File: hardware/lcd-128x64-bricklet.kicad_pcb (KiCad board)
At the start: 2 copper layers, 95 x 55 mm, 44 parts, among them P1 CON-SENSOR2, P2 Debug, P3 BOOT, P4 CON_4Wire_ER-TP028-1, Q1 2N7002, U1 XMC130024, U2 TSC2046E, U3 LCD-ERC12864, U4 DRILL, U5 DRILL, U6 DRILL, U7 DRILL

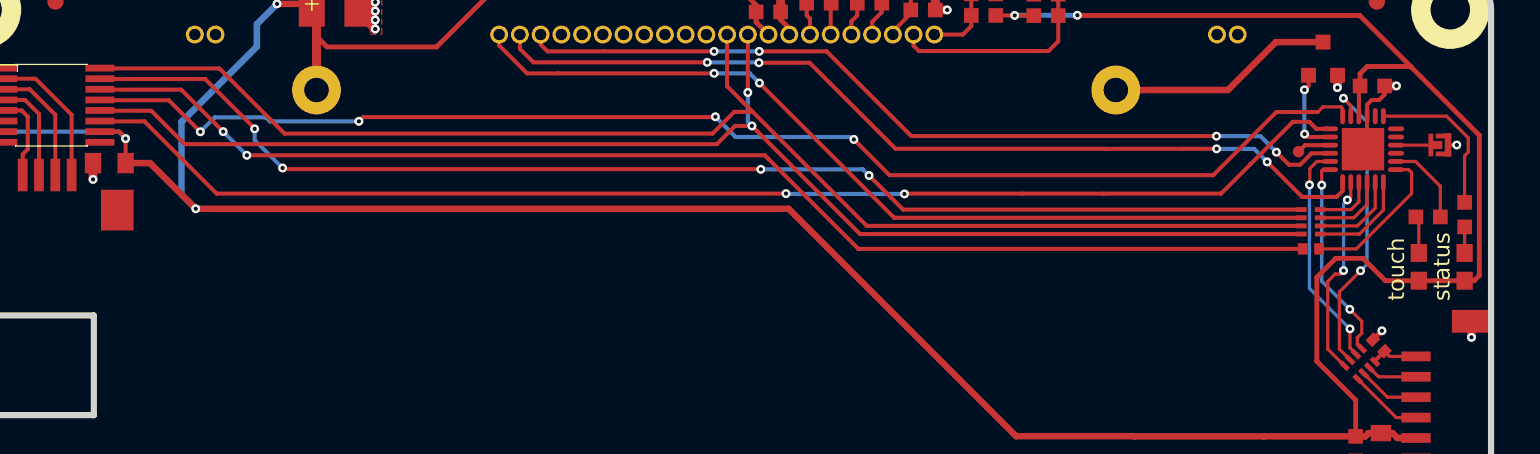
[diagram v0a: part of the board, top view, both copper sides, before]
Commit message: Change SPI pins because of flashing failure
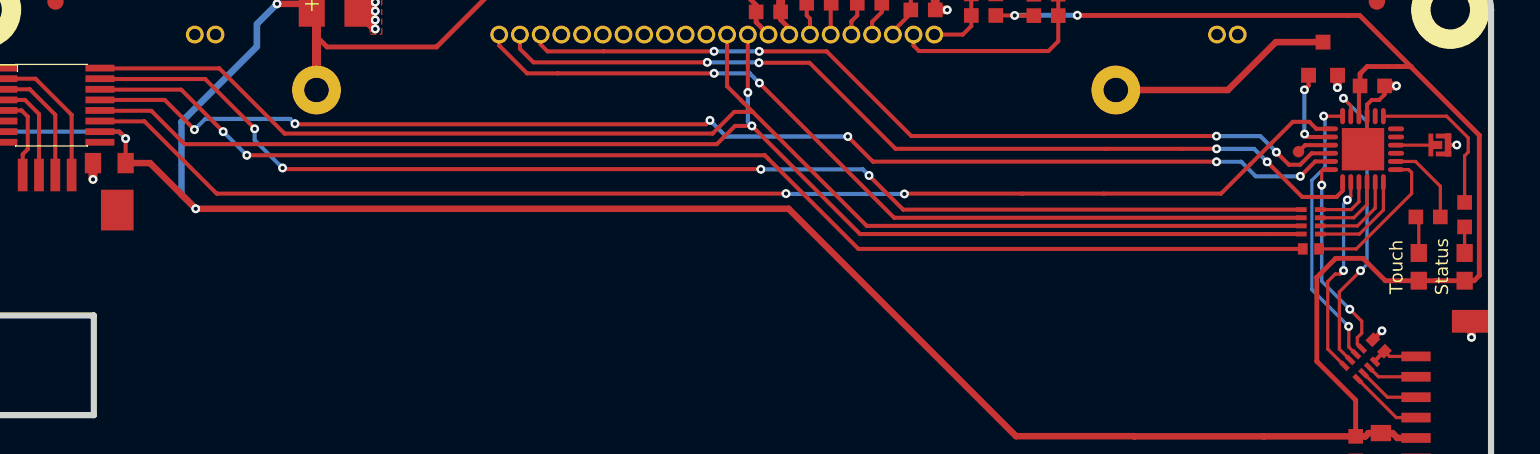
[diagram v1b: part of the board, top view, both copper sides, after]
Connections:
- U1 pad 12: TS-BUSY -> S-MOSI
- U1 pad 17: S-MOSI -> TS-BUSY
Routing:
- net S-MOSI: track 14.0 -> 17.7 mm
- net TS-BUSY: track 81.1 -> 78.5 mm, vias 4 -> 6
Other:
- board text added: "Status"
- board text added: "Touch"
- board text removed: "status"
- board text removed: "touch"
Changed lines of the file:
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@@
     (thickness 1.6)
     (drawings 16)
-    (tracks 477)
+    (tracks 479)
     (zones 0)
     (modules 44)
@@
   (title_block
     (title "LCD 128x64 Bricklet")
-    (date 2017-12-05)
+    (date 2018-01-25)
     (rev 1.0)
     (company "Tinkerforge GmbH")
     (comment 1 "Licensed under CERN OHL v.1.1")
-    (comment 2 "Copyright (©) 2017, L.Lauer <lukas@tinkerforge.com>")
+    (comment 2 "Copyright (©) 2018, L.Lauer <lukas@tinkerforge.com>")
   )
   (layers
@@
   )
   (setup
-    (last_trace_width 0.25)
+    (last_trace_width 0.2)
     (user_trace_width 0.2)
     (user_trace_width 0.25)
@@
     (visible_elements FFFFFF7F)
     (pcbplotparams
-      (layerselection 0x00030_80000001)
+      (layerselection 0x010fc_80000001)
       (usegerberextensions false)
       (excludeedgelayer true)
@@
       (psnegative false)
       (psa4output false)
-      (plotreference true)
-      (plotvalue true)
+      (plotreference false)
+      (plotvalue false)
       (plotinvisibletext false)
       (padsonsilk false)
@@
       (outputformat 1)
       (mirror false)
-      (drillshape 1)
+      (drillshape 0)
       (scaleselection 1)
       (outputdirectory ""))
@@
       (net 28 S-CLK))
     (pad 12 smd oval (at 1.25 2.025 270) (size 1 0.3) (layers F.Cu F.Paste F.Mask)
-      (net 38 TS-BUSY))
+      (net 27 S-MOSI))
     (pad 13 smd oval (at 2.025 1.25 180) (size 1 0.3) (layers F.Cu F.Paste F.Mask)
       (net 39 PENIRQ))
@@
       (net 40 LCD-CD))
     (pad 17 smd oval (at 2.025 -0.75 180) (size 1 0.3) (layers F.Cu F.Paste F.Mask)
-      (net 27 S-MOSI))
+      (net 38 TS-BUSY))
     (pad 18 smd oval (at 2.025 -1.25 180) (size 1 0.3) (layers F.Cu F.Paste F.Mask)
       (net 26 S-MISO))
@@
   (gr_line (start 101.25 88.65) (end 101.25 82.54) (angle 90) (layer Edge.Cuts) (width 0.381))
   (gr_line (start 95.25 82.54) (end 95.25 88.65) (angle 90) (layer Edge.Cuts) (width 0.381))
-  (gr_text touch (at 181.1 79.7 90) (layer F.SilkS)
-    (effects (font (size 1 1) (thickness 0.15)))
+  (gr_text Touch (at 181.1 79.57 90) (layer F.SilkS)
+    (effects (font (size 0.8 0.8) (thickness 0.15)))
   )
   (gr_text "LCD 128x64 1.0" (at 180.5 108.37) (layer F.SilkS)
@@
   (gr_arc (start 184.4 113.8) (end 186.9 113.8) (angle 90) (layer Edge.Cuts) (width 0.381))
   (gr_arc (start 184.4 63.8) (end 184.4 61.3) (angle 90) (layer Edge.Cuts) (width 0.381))
-  (gr_text status (at 183.89 79.55 90) (layer F.SilkS)
-    (effects (font (size 1 1) (thickness 0.15)))
+  (gr_text Status (at 183.89 79.55 90) (layer F.SilkS)
+    (effects (font (size 0.8 0.8) (thickness 0.15)))
   )
   (gr_arc (start 94.4 113.8) (end 94.4 116.3) (angle 90) (layer Edge.Cuts) (width 0.381))
@@
   (via (at 178.24 82.16) (size 0.55) (drill 0.25) (layers F.Cu B.Cu) (net 26))
   (segment (start 178.973249 82.893249) (end 178.24 82.16) (width 0.2) (layer F.Cu) (net 26))
+  (segment (start 177.8 70.325) (end 176.645 70.325) (width 0.2) (layer F.Cu) (net 27))
+  (segment (start 178.18 84.477974) (end 178.619427 84.917401) (width 0.2) (layer F.Cu) (net 27))
+  (segment (start 178.18 83.22) (end 178.18 84.477974) (width 0.2) (layer F.Cu) (net 27))
+  (segment (start 178.17 83.21) (end 178.18 83.22) (width 0.25) (layer F.Cu) (net 27))
+  (via (at 178.17 83.21) (size 0.55) (drill 0.25) (layers F.Cu B.Cu) (net 27))
+  (segment (start 175.91 80.95) (end 178.17 83.21) (width 0.2) (layer B.Cu) (net 27))
+  (segment (start 175.91 74.26) (end 175.91 80.95) (width 0.2) (layer B.Cu) (net 27))
+  (segment (start 176.72 73.45) (end 175.91 74.26) (width 0.2) (layer B.Cu) (net 27))
+  (segment (start 176.72 70.4) (end 176.72 73.45) (width 0.2) (layer B.Cu) (net 27))
+  (segment (start 176.64 70.32) (end 176.72 70.4) (width 0.25) (layer B.Cu) (net 27))
+  (via (at 176.64 70.32) (size 0.55) (drill 0.25) (layers F.Cu B.Cu) (net 27))
+  (segment (start 176.645 70.325) (end 176.64 70.32) (width 0.25) (layer F.Cu) (net 27))
+  (segment (start 177.8 69.96) (end 177.8 70.325) (width 0.25) (layer F.Cu) (net 27))
   (segment (start 178.619427 84.917401) (end 178.619427 84.889427) (width 0.25) (layer F.Cu) (net 27))
-  (segment (start 178.619427 84.889427) (end 178.25 84.52) (width 0.2) (layer F.Cu) (net 27))
-  (segment (start 176.23 73.1) (end 177.025 73.1) (width 0.2) (layer F.Cu) (net 27))
-  (segment (start 175.79 73.54) (end 176.23 73.1) (width 0.2) (layer F.Cu) (net 27))
-  (segment (start 175.79 74.52) (end 175.79 73.54) (width 0.2) (layer F.Cu) (net 27))
-  (segment (start 175.77 74.54) (end 175.79 74.52) (width 0.25) (layer F.Cu) (net 27))
-  (via (at 175.77 74.54) (size 0.55) (drill 0.25) (layers F.Cu B.Cu) (net 27))
-  (segment (start 175.77 80.88) (end 175.77 74.54) (width 0.2) (layer B.Cu) (net 27))
-  (segment (start 178.25 83.36) (end 175.77 80.88) (width 0.2) (layer B.Cu) (net 27))
-  (via (at 178.25 83.36) (size 0.55) (drill 0.25) (layers F.Cu B.Cu) (net 27))
-  (segment (start 178.25 84.52) (end 178.25 83.36) (width 0.2) (layer F.Cu) (net 27))
   (segment (start 178.619427 84.917401) (end 178.619427 84.899427) (width 0.2) (layer F.Cu) (net 27))
   (segment (start 178.267401 85.269427) (end 178.267401 85.267401) (width 0.25) (layer F.Cu) (net 28))
@@
   (segment (start 177.425 75.275) (end 175.325 75.275) (width 0.25) (layer F.Cu) (net 37))
   (segment (start 177.8 74.9) (end 177.425 75.275) (width 0.25) (layer F.Cu) (net 37))
-  (segment (start 117.5 70.64) (end 112.04 70.64) (width 0.25) (layer B.Cu) (net 38))
-  (segment (start 108.66 70.4) (end 107.78 71.28) (width 0.25) (layer B.Cu) (net 38))
-  (segment (start 111.8 70.4) (end 108.66 70.4) (width 0.25) (layer B.Cu) (net 38))
-  (segment (start 112.04 70.64) (end 111.8 70.4) (width 0.25) (layer B.Cu) (net 38))
-  (segment (start 177.8 70.325) (end 177.8 69.855002) (width 0.2) (layer F.Cu) (net 38))
-  (segment (start 177.8 69.855002) (end 177.7 69.755002) (width 0.2) (layer F.Cu) (net 38))
-  (segment (start 176.594998 69.755002) (end 176.28 70.07) (width 0.2) (layer F.Cu) (net 38))
-  (segment (start 177.7 69.755002) (end 176.594998 69.755002) (width 0.2) (layer F.Cu) (net 38))
-  (segment (start 150.03 73.94) (end 147.84 71.75) (width 0.25) (layer F.Cu) (net 38))
-  (segment (start 169.87 73.94) (end 150.03 73.94) (width 0.25) (layer F.Cu) (net 38))
-  (segment (start 173.74 70.07) (end 169.87 73.94) (width 0.25) (layer F.Cu) (net 38))
-  (segment (start 176.28 70.07) (end 173.74 70.07) (width 0.25) (layer F.Cu) (net 38))
-  (via (at 147.84 71.75) (size 0.55) (drill 0.25) (layers F.Cu B.Cu) (net 38))
-  (segment (start 101.82434 69.34742) (end 105.84742 69.34742) (width 0.25) (layer F.Cu) (net 38))
-  (via (at 107.78 71.28) (size 0.55) (drill 0.25) (layers F.Cu B.Cu) (net 38))
-  (segment (start 107.78 71.28) (end 105.84742 69.34742) (width 0.25) (layer F.Cu) (net 38))
-  (via (at 117.5 70.64) (size 0.55) (drill 0.25) (layers F.Cu B.Cu) (net 38))
-  (segment (start 117.76 70.38) (end 117.5 70.64) (width 0.25) (layer F.Cu) (net 38))
-  (segment (start 139.33 70.38) (end 117.76 70.38) (width 0.25) (layer F.Cu) (net 38))
-  (segment (start 139.35 70.36) (end 139.33 70.38) (width 0.25) (layer F.Cu) (net 38))
-  (via (at 139.35 70.36) (size 0.55) (drill 0.25) (layers F.Cu B.Cu) (net 38))
-  (segment (start 140.59 71.6) (end 139.35 70.36) (width 0.25) (layer B.Cu) (net 38))
-  (segment (start 147.69 71.6) (end 140.59 71.6) (width 0.25) (layer B.Cu) (net 38))
-  (segment (start 147.69 71.6) (end 147.84 71.75) (width 0.25) (layer B.Cu) (net 38))
-  (segment (start 147.84 71.75) (end 147.83 71.75) (width 0.25) (layer F.Cu) (net 38))
+  (segment (start 101.62434 69.32742) (end 105.59742 69.32742) (width 0.25) (layer F.Cu) (net 38))
+  (segment (start 176.12 73.1) (end 177.025 73.1) (width 0.25) (layer F.Cu) (net 38))
+  (segment (start 175.21 74.01) (end 176.12 73.1) (width 0.25) (layer F.Cu) (net 38))
+  (via (at 175.21 74.01) (size 0.55) (drill 0.25) (layers F.Cu B.Cu) (net 38))
+  (segment (start 172.48 74.01) (end 175.21 74.01) (width 0.25) (layer B.Cu) (net 38))
+  (segment (start 171.59 73.12) (end 172.48 74.01) (width 0.25) (layer B.Cu) (net 38))
+  (segment (start 170.07 73.12) (end 171.59 73.12) (width 0.25) (layer B.Cu) (net 38))
+  (via (at 170.07 73.12) (size 0.55) (drill 0.25) (layers F.Cu B.Cu) (net 38))
+  (segment (start 170.06 73.11) (end 170.07 73.12) (width 0.25) (layer F.Cu) (net 38))
+  (segment (start 149.01 73.11) (end 170.06 73.11) (width 0.25) (layer F.Cu) (net 38))
+  (segment (start 147.47 71.57) (end 149.01 73.11) (width 0.25) (layer F.Cu) (net 38))
+  (via (at 147.47 71.57) (size 0.55) (drill 0.25) (layers F.Cu B.Cu) (net 38))
+  (segment (start 140.01 71.57) (end 147.47 71.57) (width 0.25) (layer B.Cu) (net 38))
+  (segment (start 139.02 70.58) (end 140.01 71.57) (width 0.25) (layer B.Cu) (net 38))
+  (via (at 139.02 70.58) (size 0.55) (drill 0.25) (layers F.Cu B.Cu) (net 38))
+  (segment (start 138.78 70.82) (end 139.02 70.58) (width 0.25) (layer F.Cu) (net 38))
+  (segment (start 113.61 70.82) (end 138.78 70.82) (width 0.25) (layer F.Cu) (net 38))
+  (segment (start 113.58 70.79) (end 113.61 70.82) (width 0.25) (layer F.Cu) (net 38))
+  (via (at 113.58 70.79) (size 0.55) (drill 0.25) (layers F.Cu B.Cu) (net 38))
+  (segment (start 113.28 70.49) (end 113.58 70.79) (width 0.25) (layer B.Cu) (net 38))
+  (segment (start 108.08 70.49) (end 113.28 70.49) (width 0.25) (layer B.Cu) (net 38))
+  (segment (start 107.42 71.15) (end 108.08 70.49) (width 0.25) (layer B.Cu) (net 38))
+  (via (at 107.42 71.15) (size 0.55) (drill 0.25) (layers F.Cu B.Cu) (net 38))
+  (segment (start 105.59742 69.32742) (end 107.42 71.15) (width 0.25) (layer F.Cu) (net 38))
   (segment (start 172.14 73.28) (end 173.43 71.99) (width 0.25) (layer F.Cu) (net 39))
   (segment (start 101.72434 70.64282) (end 104.35282 70.64282) (width 0.25) (layer F.Cu) (net 39))
